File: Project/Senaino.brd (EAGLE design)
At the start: 68.6 x 53.3 mm, 34 parts, among them Q1 16 MHz, U1 ATMEGA328P-PU, U2 FT232RL, U3 7805T

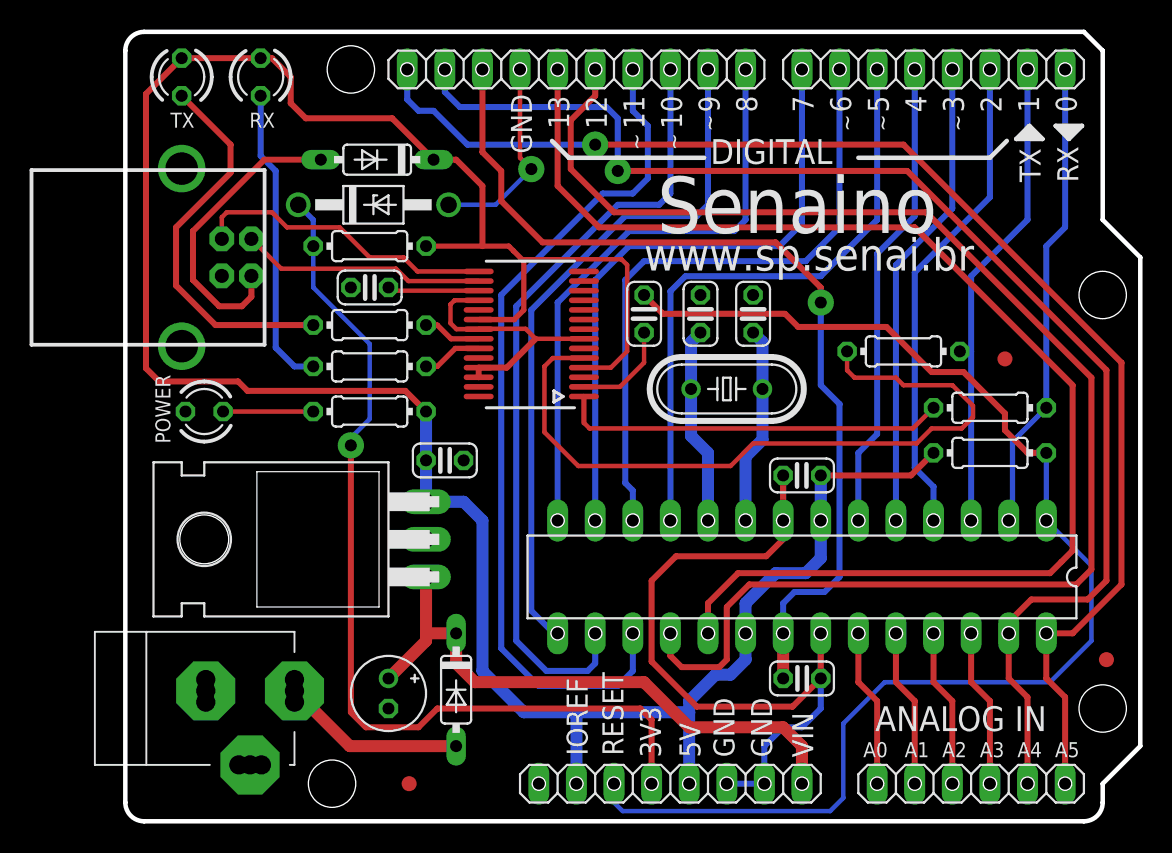
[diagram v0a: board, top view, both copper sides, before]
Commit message: USB/Serial Converter Chip Change
- The FT232 USB/Serial converter changed by CH340.

- The reason for this is to create a second alternative to FT232 converter. This is not always available in large quantities in the Brazilian market.

- In addition, CH340 encapsulation is easier to solder on the board.
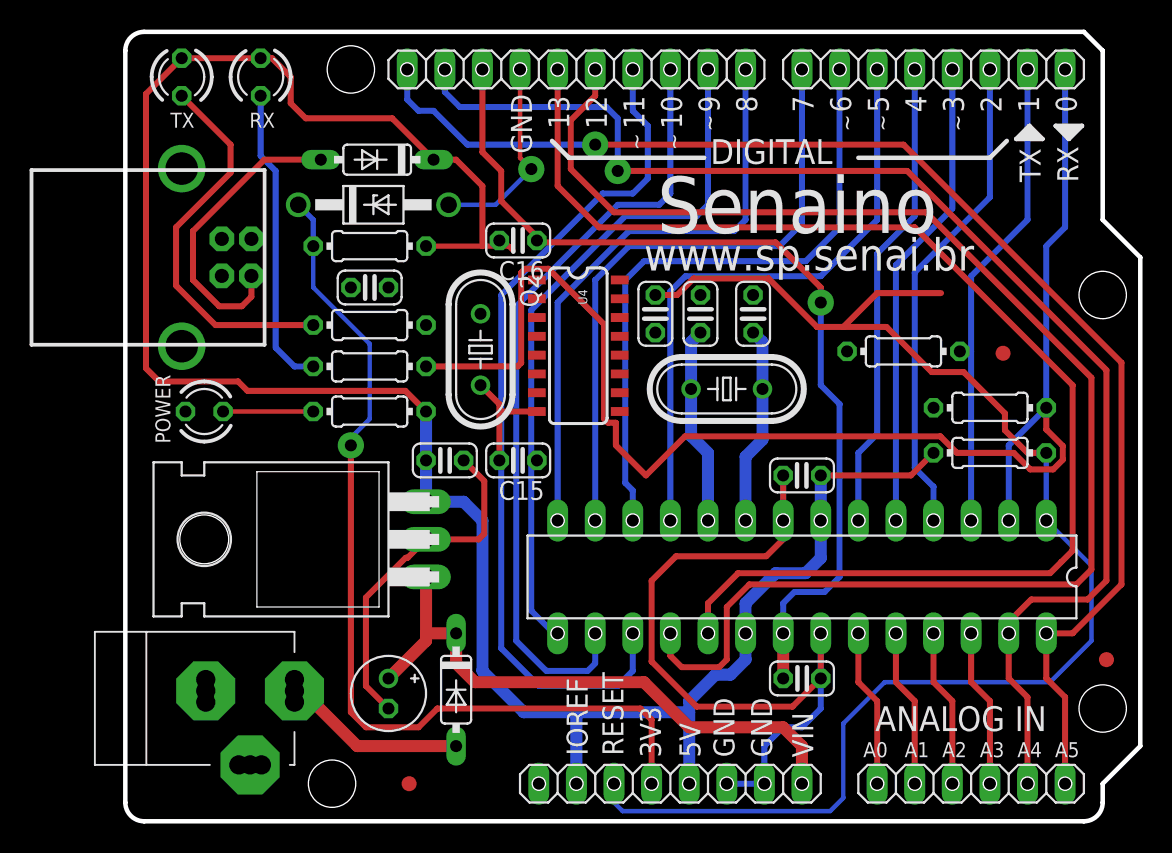
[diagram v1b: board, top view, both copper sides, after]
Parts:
- removed U2: FT232RL, MySMD2:SSOP28
- added C15, C16: 22 pF, rcl:C025-024X044
- added Q2: 12 MHz, crystal:HC49/S
- added U4: CH340G, Serial-Basic:SO016
- moved C3 0.76 mm to (35.8, 34.3)
- moved FD1 0.40 mm to (59.3, 31.6)
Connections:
- removed net N$14: U2.8
- removed net N$15: U2.9
- removed net N$16: U2.10
- removed net N$17: U2.28
- removed net N$18: U2.27
- removed net N$19: U2.24
- removed net N$20: U2.13
- removed net N$21: U2.14
- removed net N$22: U2.12
- removed net N$23: U2.19
- removed net N$27: U2.3
- removed net RX: R7.1, U2.1
- removed net TX: R6.1, U2.5
- new net PE: C15.1, C16.1, U4.1
- net +5V: now also U4.16; no longer U2.20, U2.4
- net D0: now also R3.1
- net D1: now also R4.1
- net GND: no longer U2.18, U2.21, U2.25, U2.26, U2.7
- net N$10: now also R7.1, U4.3; no longer R4.1, U2.22
- net N$11: now also U4.4; no longer U2.17
- net N$12: now also C15.2, Q2.2, U4.8; no longer U2.11
- net N$13: now also C16.2, Q2.1, U4.7; no longer U2.6
- net N$2: now also U4.5, X2.3; no longer U2.16, X2.2
- net N$3: now also U4.13; no longer U2.2
- net N$4: now also R6.1, U4.2; no longer R3.1, U2.23
- net N$5: now also U4.6, X2.2; no longer U2.15, X2.3
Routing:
- net D0: track 32.1 -> 98.1 mm
- net TX: track 50.2 -> 0.00 mm
- net +5V: track 179.5 -> 152.2 mm
- net RX: track 26.1 -> 0.00 mm
- net N$5: track 20.6 -> 0.00 mm
- net N$2: track 16.5 -> 0.00 mm
- net N$12: track 0.00 -> 8.19 mm
- net RESET: track 87.7 -> 95.4 mm
- net N$3: track 6.77 -> 0.00 mm
- net N$11: track 6.19 -> 0.00 mm
- net GND: track 85.6 -> 91.0 mm
- net N$4: track 4.06 -> 0.00 mm
- net N$10: track 3.94 -> 0.00 mm
- net D1: track 32.8 -> 32.1 mm
